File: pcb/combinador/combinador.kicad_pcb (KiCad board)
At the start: 2 copper layers, 140 x 35 mm, 17 parts, among them J1 SMA, J2 SMA, J3 SMA, J4 SMA, J5 SMA, J6 SMA, U1 1.7GHz, U2 2.5GHz, U3 3.5GHz, U4 4.1GHz

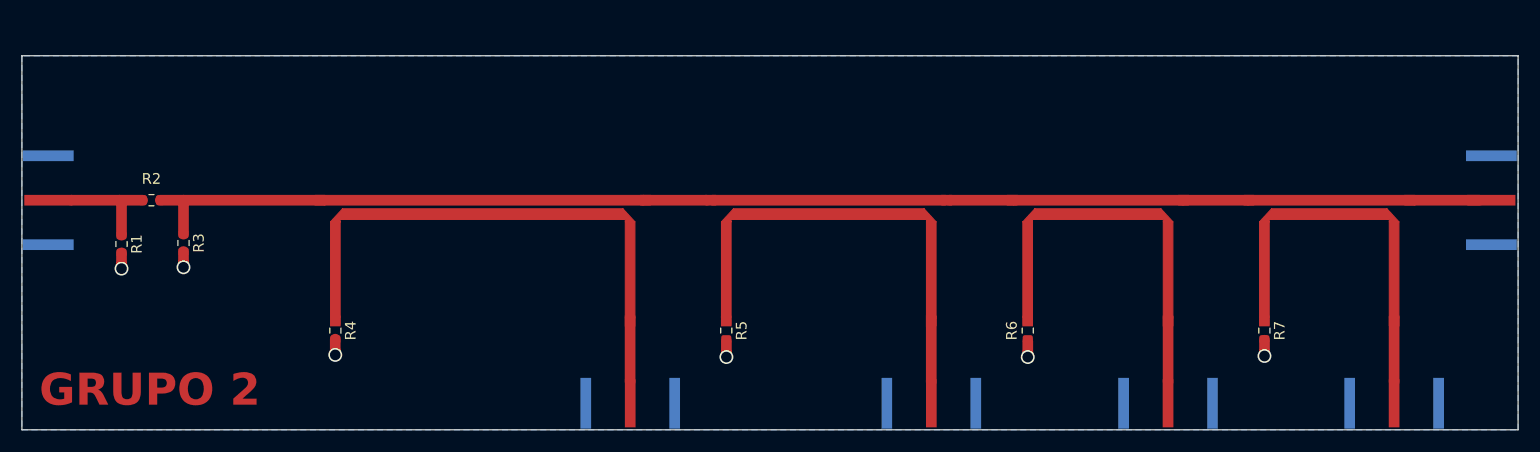
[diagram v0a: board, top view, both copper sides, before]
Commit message: Actualización
Agregado de modelo 3d de conectores, correxión en la medida de los pads de los resistores. Agregado de etiquetas de cada acoplador.
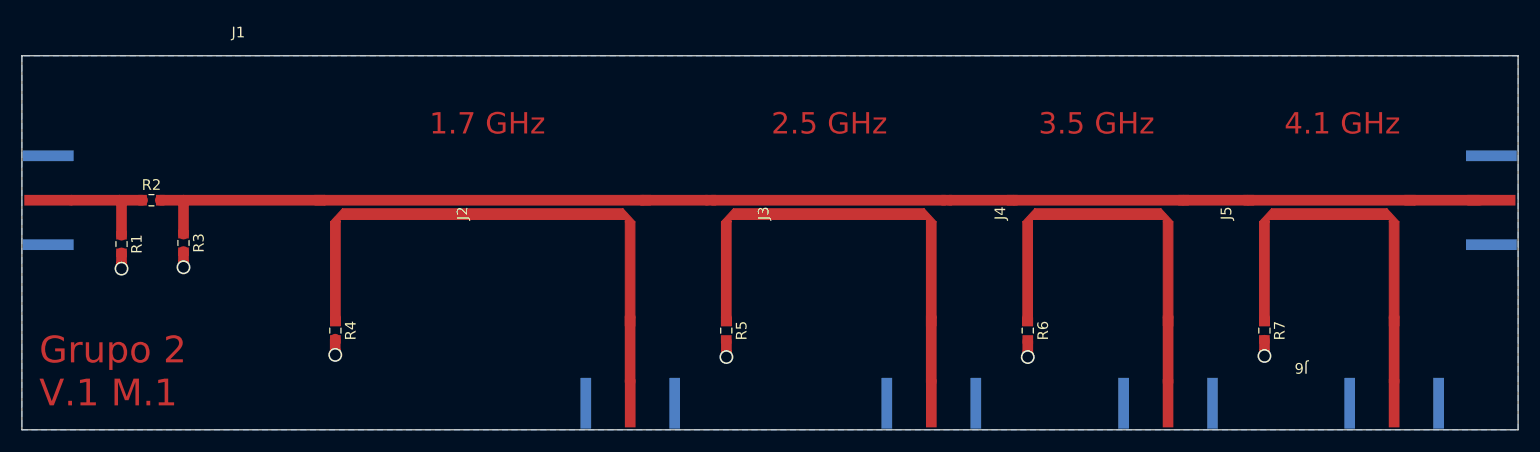
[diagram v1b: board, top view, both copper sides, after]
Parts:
- J1, J2, J3, J4, J5, J6: footprint footprint_project_library:SMA -> footprint_project_library:SMA_horizontal_microstrip
- R1, R2, R3, R4, R5, R6, R7: footprint Resistor_SMD:R_0603_1608Metric -> footprint_project_library:R_0603
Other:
- board text added: "1.7 GHz"
- board text added: "2.5 GHz"
- board text added: "3.5 GHz"
- board text added: "4.1 GHz"
- board text added: "Grupo 2 V.1 M.1"
- board text removed: "GRUPO 2"

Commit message: Actualización
Cambio de etiquetas de conectores
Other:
- board text added: "0.9 GHz"
